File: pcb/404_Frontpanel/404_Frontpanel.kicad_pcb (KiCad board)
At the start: 2 copper layers, 54.5 x 106.4 mm, 11 parts

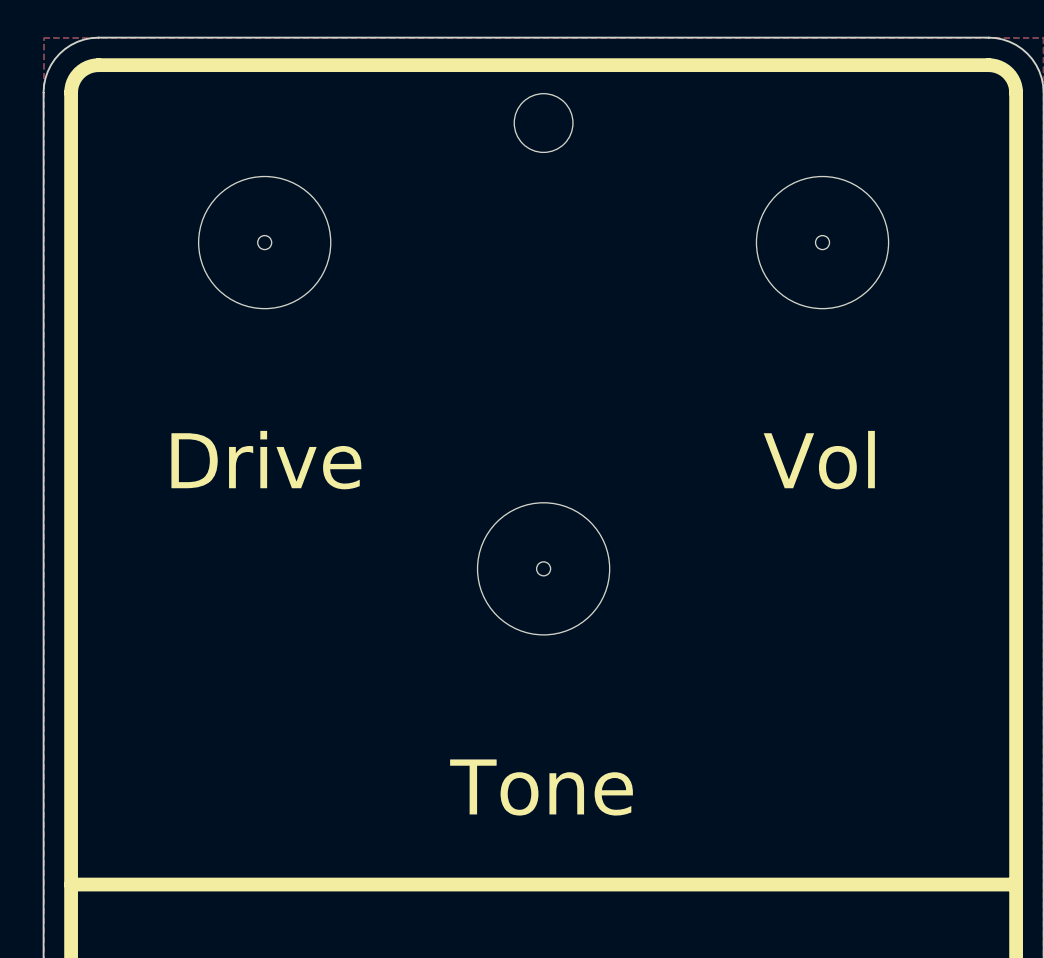
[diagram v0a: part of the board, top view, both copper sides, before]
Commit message: [404] Recreate Upper and Front PCBs according to new base templates
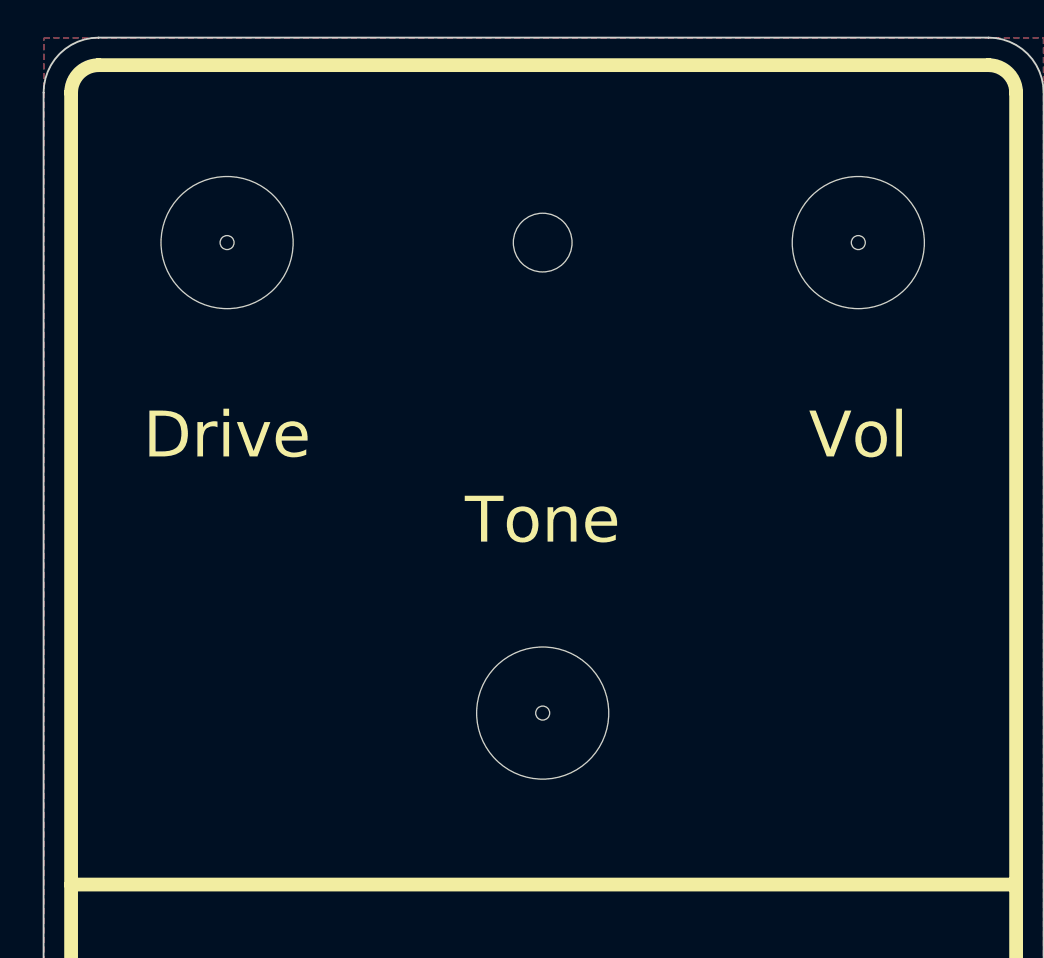
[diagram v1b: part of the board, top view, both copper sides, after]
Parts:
- moved Tone 7.86 mm to (149.4, 95.3), turned to 180 degrees
- moved MK2 6.52 mm to (149.4, 69.6), turned to 180 degrees
- moved Drive 2.05 mm to (132.2, 69.6)
- moved Vol 1.95 mm to (166.7, 69.6)
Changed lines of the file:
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@@
     (pad_to_mask_clearance 0.05)
     (solder_mask_min_width 0.254)
-    (aux_axis_origin 149.5 63.13)
-    (grid_origin 172.25 119.63)
+    (aux_axis_origin 149.45 69.645)
+    (grid_origin 149.45 69.645)
     (pcbplotparams
       (layerselection 0x00010fc_ffffffff)
@@
   )
   (footprint "MeineBib:Drill_9mmPot_7,2mm" (layer "F.Cu")
-    (at 134.3 69.645)
-    (attr board_only exclude_from_pos_files exclude_from_bom)
-    (fp_text reference "Drive" (at 0 12 unlocked) (layer "F.SilkS")
-      (effects (font (size 3 3) (thickness 0.5)))
+    (at 132.25 69.645)
+    (attr board_only exclude_from_pos_files exclude_from_bom)
+    (fp_text reference "Drive" (at 0 10.5) (layer "F.SilkS")
+      (effects (font (size 2.5 2.5) (thickness 0.5)))
     )
     (fp_text value "Drill_9mmPot_7,2mm" (at 0 1 unlocked) (layer "F.Fab") hide
@@
       (effects (font (size 1 1) (thickness 0.15)))
     )
-    (pad "" np_thru_hole circle (at 0 0) (size 14 14) (drill 0.762) (layers *.Mask))
+    (fp_text user "16mm pot" (at 0 7 unlocked) (layer "User.1")
+      (effects (font (size 1 1) (thickness 0.15)))
+    )
+    (fp_circle (center 0 0) (end 8 0) (layer "F.Fab") (width 0.12) (fill none))
     (pad "" np_thru_hole circle (at 0 0) (size 7.2 7.2) (drill 7.2) (layers *.Mask)
       (clearance 3.6))
+    (pad "" np_thru_hole circle (at 0 0) (size 14 14) (drill 0.762) (layers *.Mask))
   )
   (footprint "MeineBib:EigenesMountingHole_3.2mm_M3_Small" (layer "F.Cu")
@@
   )
   (footprint "MeineBib:Drill_9mmPot_7,2mm" (layer "F.Cu")
-    (at 149.5 87.425)
-    (attr board_only exclude_from_pos_files exclude_from_bom)
-    (fp_text reference "Tone" (at 0 12 unlocked) (layer "F.SilkS")
-      (effects (font (size 3 3) (thickness 0.5)))
-    )
-    (fp_text value "Drill_9mmPot_7,2mm" (at 0 1 unlocked) (layer "F.Fab") hide
-      (effects (font (size 1 1) (thickness 0.15)))
-    )
-    (fp_text user "${REFERENCE}" (at 0 2.5 unlocked) (layer "F.Fab") hide
-      (effects (font (size 1 1) (thickness 0.15)))
-    )
-    (pad "" np_thru_hole circle (at 0 0) (size 14 14) (drill 0.762) (layers *.Mask))
-    (pad "" np_thru_hole circle (at 0 0) (size 7.2 7.2) (drill 7.2) (layers *.Mask)
+    (at 149.45 95.285 180)
+    (attr board_only exclude_from_pos_files exclude_from_bom)
+    (fp_text reference "Tone" (at 0 10.5 180) (layer "F.SilkS")
+      (effects (font (size 2.5 2.5) (thickness 0.5)))
+    )
+    (fp_text value "Drill_9mmPot_7,2mm" (at 0 1 180 unlocked) (layer "F.Fab") hide
+      (effects (font (size 1 1) (thickness 0.15)))
+    )
+    (fp_text user "${REFERENCE}" (at 0 2.5 180 unlocked) (layer "F.Fab") hide
+      (effects (font (size 1 1) (thickness 0.15)))
+    )
+    (fp_text user "16mm pot" (at 0 7 180 unlocked) (layer "User.1")
+      (effects (font (size 1 1) (thickness 0.15)))
+    )
+    (fp_circle (center 0 0) (end 8 0) (layer "F.Fab") (width 0.12) (fill none))
+    (pad "" np_thru_hole circle (at 0 0 180) (size 7.2 7.2) (drill 7.2) (layers *.Mask)
       (clearance 3.6))
+    (pad "" np_thru_hole circle (at 0 0 180) (size 14 14) (drill 0.762) (layers *.Mask))
   )
   (footprint "MeineBib:EigenesMountingHole_3.2mm_M3_Small" (layer "F.Cu")
@@
   )
   (footprint "MeineBib:EigenesMountingHole_3.2mm_M3_Small" (layer "F.Cu")
-    (at 149.5 63.13)
+    (at 149.45 69.645 180)
     (descr "Mounting Hole 2.7mm, no annular, M2.5")
     (tags "mounting hole 2.7mm no annular m2.5")
@@
     (fp_circle (center 0 0) (end 3.1 0) (layer "Cmts.User") (width 0.15) (fill none))
     (fp_circle (center 0 0) (end 3.1 0) (layer "F.CrtYd") (width 0.05) (fill none))
-    (pad "" np_thru_hole circle (at 0 0) (size 3.2 3.2) (drill 3.2) (layers F&B.Cu *.Mask)
+    (pad "" np_thru_hole circle (at 0 0 180) (size 3.2 3.2) (drill 3.2) (layers F&B.Cu *.Mask)
       (solder_mask_margin 1.65) (clearance 1.8))
   )
   (footprint "MeineBib:Drill_9mmPot_7,2mm" (layer "F.Cu")
-    (at 164.7 69.645)
-    (attr board_only exclude_from_pos_files exclude_from_bom)
-    (fp_text reference "Vol" (at 0 12 unlocked) (layer "F.SilkS")
-      (effects (font (size 3 3) (thickness 0.5)))
+    (at 166.65 69.645)
+    (attr board_only exclude_from_pos_files exclude_from_bom)
+    (fp_text reference "Vol" (at 0 10.5) (layer "F.SilkS")
+      (effects (font (size 2.5 2.5) (thickness 0.5)))
     )
     (fp_text value "Drill_9mmPot_7,2mm" (at 0 1 unlocked) (layer "F.Fab") hide
@@
       (effects (font (size 1 1) (thickness 0.15)))
     )
+    (fp_text user "16mm pot" (at 0 7 unlocked) (layer "User.1")
+      (effects (font (size 1 1) (thickness 0.15)))
+    )
+    (fp_circle (center 0 0) (end 8 0) (layer "F.Fab") (width 0.12) (fill none))
     (pad "" np_thru_hole circle (at 0 0) (size 14 14) (drill 0.762) (layers *.Mask))
     (pad "" np_thru_hole circle (at 0 0) (size 7.2 7.2) (drill 7.2) (layers *.Mask)

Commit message: [404] Fix frontpanel pent location
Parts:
- moved MK6 5.87 mm to (149.5, 78.6)
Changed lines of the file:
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@@
       (excludeedgelayer true)
       (plotframeref false)
-      (viasonmask false)
+      (viasonmask true)
       (mode 1)
-      (useauxorigin true)
+      (useauxorigin false)
       (hpglpennumber 1)
       (hpglpenspeed 20)
@@
   )
   (footprint "MeineBib:PentThin" (layer "B.Cu")
-    (at 149.450706 72.767826 180)
+    (at 149.450706 78.635826 180)
     (attr exclude_from_pos_files exclude_from_bom)
     (fp_text reference "MK6" (at 0 0) (layer "B.SilkS") hide
